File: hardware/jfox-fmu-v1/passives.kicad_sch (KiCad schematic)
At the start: 62 parts, among them X1 16MHz, X2 32.768kHz

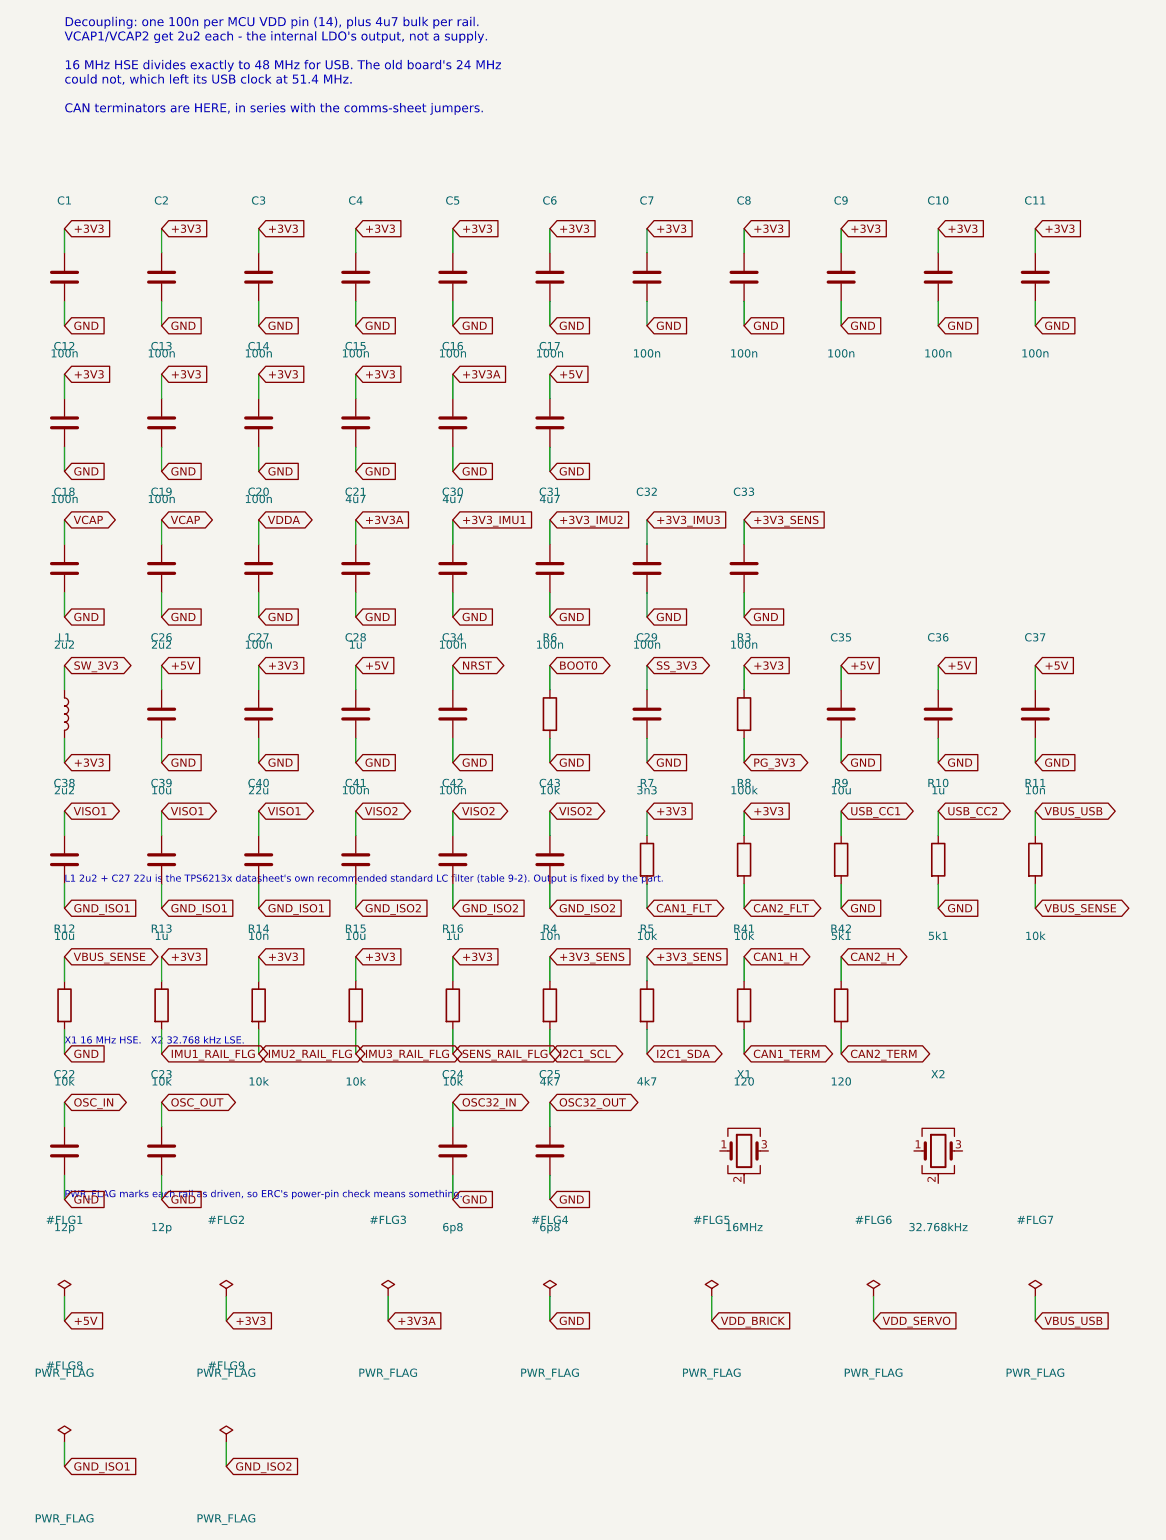
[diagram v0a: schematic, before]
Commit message: Connectors, and three more wires that went nowhere
Eleven headers on a new sheet, Pixhawk pinouts on JST-GH 1.25 mm: two TELEM,
two GPS, RC, a 10-way debug, external SPI, both power inputs, safety switch,
and the eight PWM channels. Pixhawk's pinout rather than a novel one because
the ecosystem's GPS units, radios and power modules are built to it, and a
different pinout means a custom loom for every peripheral.

Isolated nets 48 -> 10.

Three more defects found on the way, all the same shape as the last batch -
something that looked wired and was not:

  C20 decoupled a net called "VDDA" that nothing else joined. The MCU's VDDA
  pin is on +3V3A. The analog rail's bypass capacitor was connected to
  nothing at all.

  LED_R/G/B had MCU pins allocated and drove nothing - the board had no way
  to say anything. Now three LEDs with series resistors, common anode.

  And the two_pin helper assumed every two-pin part is drawn vertically. It
  splits the pins on dy < 0, but Device:LED is horizontal with both pins at
  dy = 0, so both took the same net: D1 shorted its own anode to its cathode
  while the anode net kept only the series resistor. It looked wired and was
  a short. Now split on whichever axis actually separates the pins.

The debug header went from 6 ways to 10. Six could carry SWD and USART1_TX
but not RX, so the console would have been write-only.

Worth recording: when the passives sheet outgrew A4 mid-change, the generator
correctly refused to write - and every checker then passed against the
PREVIOUS generation still on disk. Green on stale files. The fix was to
re-lay-out and regenerate before trusting any of it, but the trap is real and
worth knowing about.

Remaining 10 isolated nets are honest and all blocked on the same two things:
UV1-3_SET and OV1-3_SET need the LTC4417's threshold equations, PGATE1-3 need
its external PMOS pass devices, and both need the datasheet, which would not
download in this session. SD_DETECT needs a socket symbol that ex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
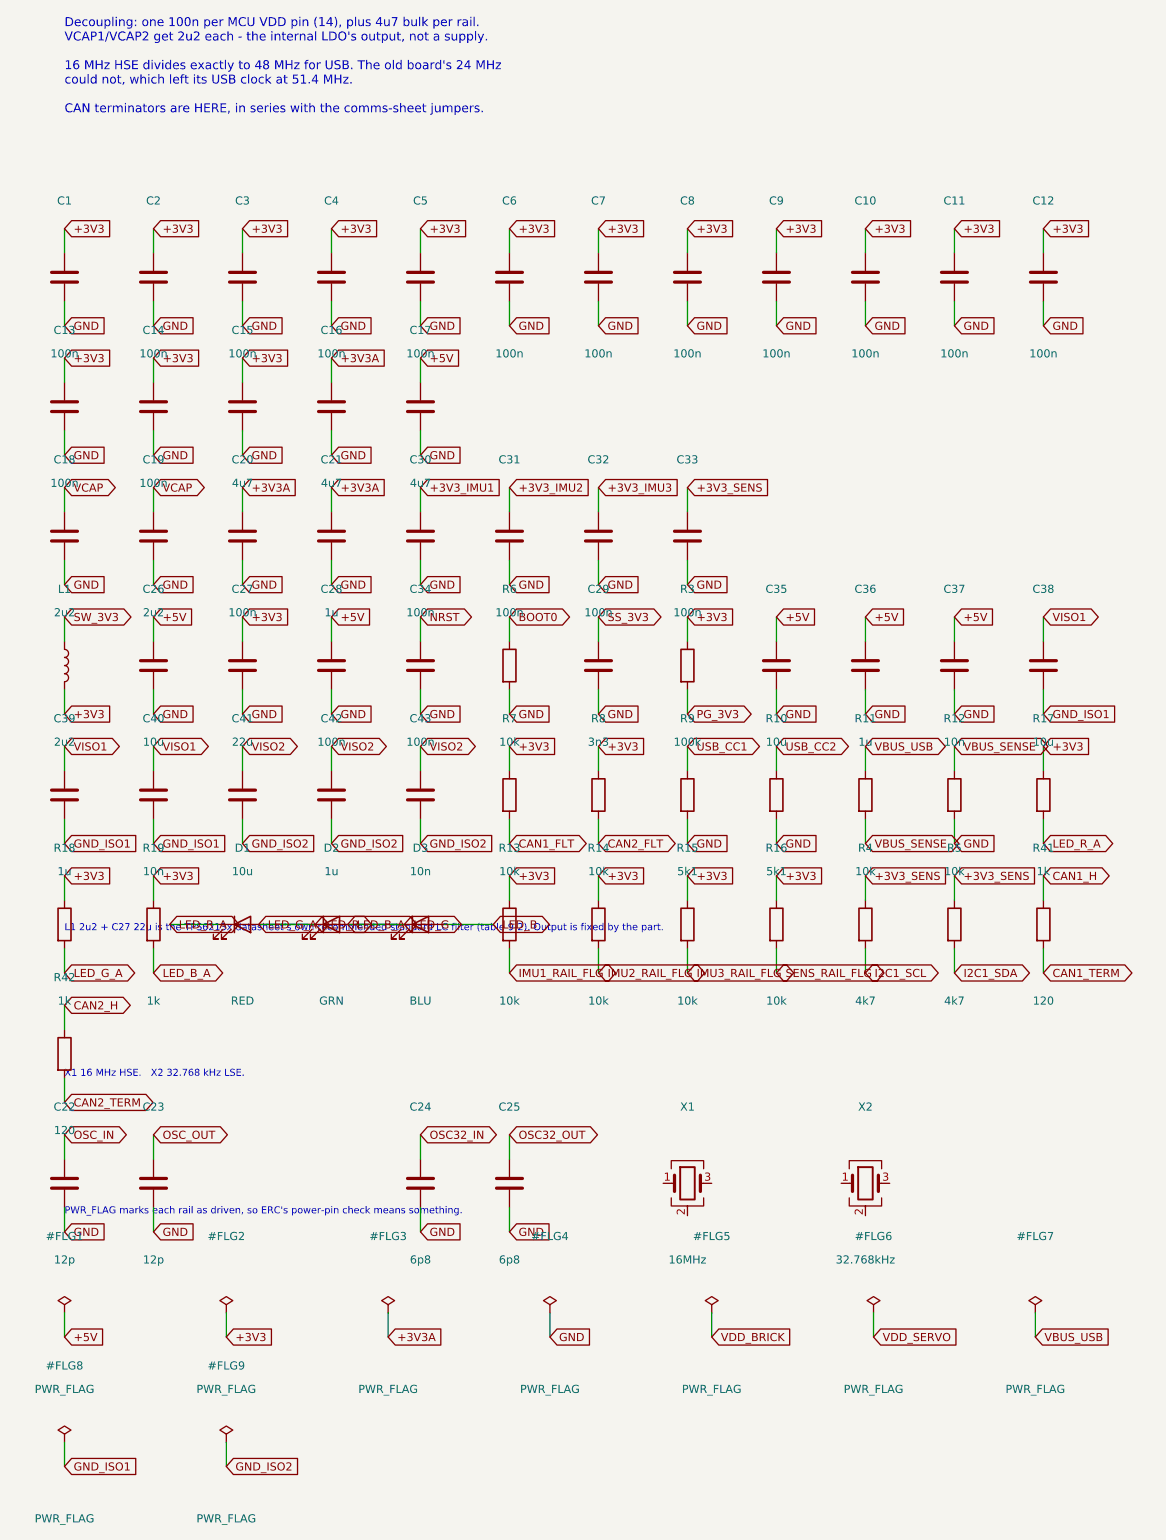
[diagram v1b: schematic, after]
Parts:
- added D1: RED, LED_SMD:LED_0603_1608Metric, symbol Device:LED
- added D2: GRN, LED_SMD:LED_0603_1608Metric, symbol Device:LED
- added D3: BLU, LED_SMD:LED_0603_1608Metric, symbol Device:LED
- added R17, R18, R19: 1k, Resistor_SMD:R_0402_1005Metric, symbol Device:R
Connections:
- net VDDA is gone; now on net +3V3A: C20.1
- net +3V3: now also R17.1, R18.1, R19.1
- new net LED_B: D3.2 (A)
- new net LED_B_A: D2.2 (A), D3.1 (K), R19.2
- new net LED_G_A: D1.2 (A), D2.1 (K), R18.2
- new net LED_R_A: D1.1 (K), R17.2

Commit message: The ORing controller had no switches and no thresholds
With the LTC4417 datasheet in hand, the last of the connections close.
Isolated nets 10 -> 1.

PGATE1-3 drove nothing and UV/OV_SET went nowhere, so U20 sat on the board
arbitrating between three inputs it could neither measure nor switch. Both
halves are now built:

Two back-to-back PMOS per input, sources common, gates both on Gn. That is
what "blocks reverse AND cross conduction" on the datasheet's front page
actually requires - one FET's body diode faces each way. A single FET per
channel leaves a permanent diode path and the ORing does nothing.

And VS1-3 were wired straight to the input rails. VSn senses the FET common
source (ADI figure 1), so the design was measuring the wrong side of a switch
that did not exist.

Thresholds from ADI's equations, with UV taking the middle tap and OV the
bottom one:

    UV = Rtot / (Rmid + Rbot)        OV = Rtot / Rbot

Checked by reproducing the datasheet's own worked example before using them:
806k/39.2k/60.4k gives 9.09 V and 14.99 V, which is what figure 1 labels for a
12 V adapter. Then applied per input - brick 4.52/5.81 V, servo 4.54/6.55 V
because BECs are commonly 5 V or 6 V, USB 4.38/5.47 V.

Two BOM errors the datasheet also settled:

The LTC4417 is a 24-lead part. It carried Package_SO:SSOP-16 - a real
footprint, a real name, eight pads short, and unbuildable. check_fmu_footprints
was verifying that a name RESOLVES, never that it matches the part, so this
passed every run. It now compares pad count against pin count.

That check concealed itself twice while being written, in the way this file
has form for: `mismatched` was not added to the total, so the count silently
dropped by one and printed PASS; then `good` did not include it either, so it
printed FAIL and exited 0. Both fixed, and the total now carries a comment
saying why every failure category must be in it.

And the datasheet's ordering table lists only I (-40/+85) and H (-40/+125)
grades - there is 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
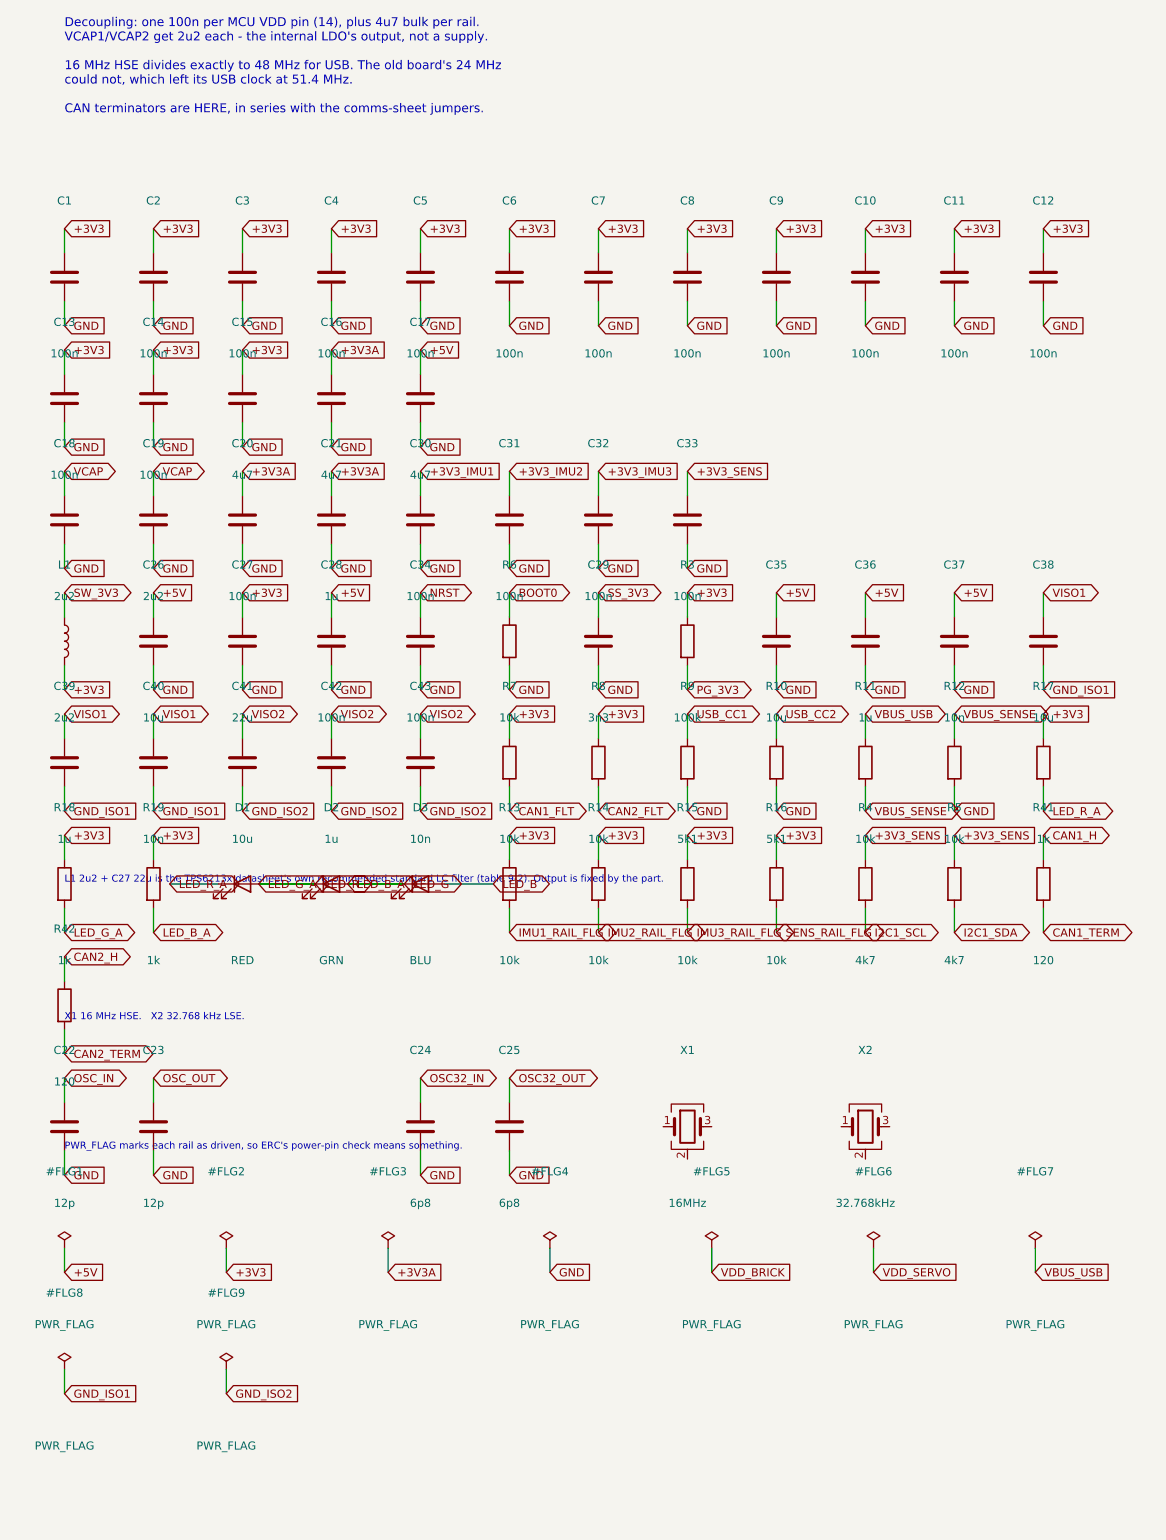
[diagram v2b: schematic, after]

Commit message: microSD with card detect, and the storage split made explicit
The socket was already on the board and every SDMMC line was wired, but it
used Connector:SD_Card_Device - a symbol with no card-detect pin and no
shield. SD_DETECT therefore had an MCU pin allocated and no source, and the
shield floated.

Swapped to Connector:Micro_SD_Card_Det_Hirose_DM3AT, which is the same socket
the footprint was already chosen for and exposes the DET_A/DET_B mechanical
switch plus SHIELD. DET_B grounds, DET_A is pulled up and read, so firmware
can tell "no card" from "card present but failing". Those need different
responses - the first is a pre-flight nag, the second is a logging fault - and
without card detect they are indistinguishable.

Six pull-ups added. The SD specification requires CMD and DAT0-3 held high,
and DAT3 doubles as the card's own detect pin so it must not float during
initialisation. The STM32's internal pull-ups exist but are weak and only
come up after GPIO configuration, which is after the card has already sampled
the bus.

Isolated nets: 1 -> 0. Every net on this board now reaches at least two pins.

On what the card is FOR, since the request was about parameters: it is not
where parameters go, and it should not be.

Parameters and calibration stay in the FM25V02A FRAM, which is where
flight::calibration::storage already writes them - with a "JFOX" magic word
and an FNV-1a checksum so a blank or corrupted record can never read as
valid. FRAM has unlimited write endurance, needs no filesystem, and cannot be
corrupted by power loss mid-write. An SD card can be pulled out, wears out,
and corrupts on power loss during a block write. Putting calibration there
would be a downgrade dressed as convenience.

The card is for flight logs: large, sequential, expendable - the opposite of
parameters, and exactly what the medium is good at. HWR-IFC-006 now says
FRAM explicitly rather than "non-volatile storage", and HWR-IFC-007 covers
the socket, so the distinction is record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
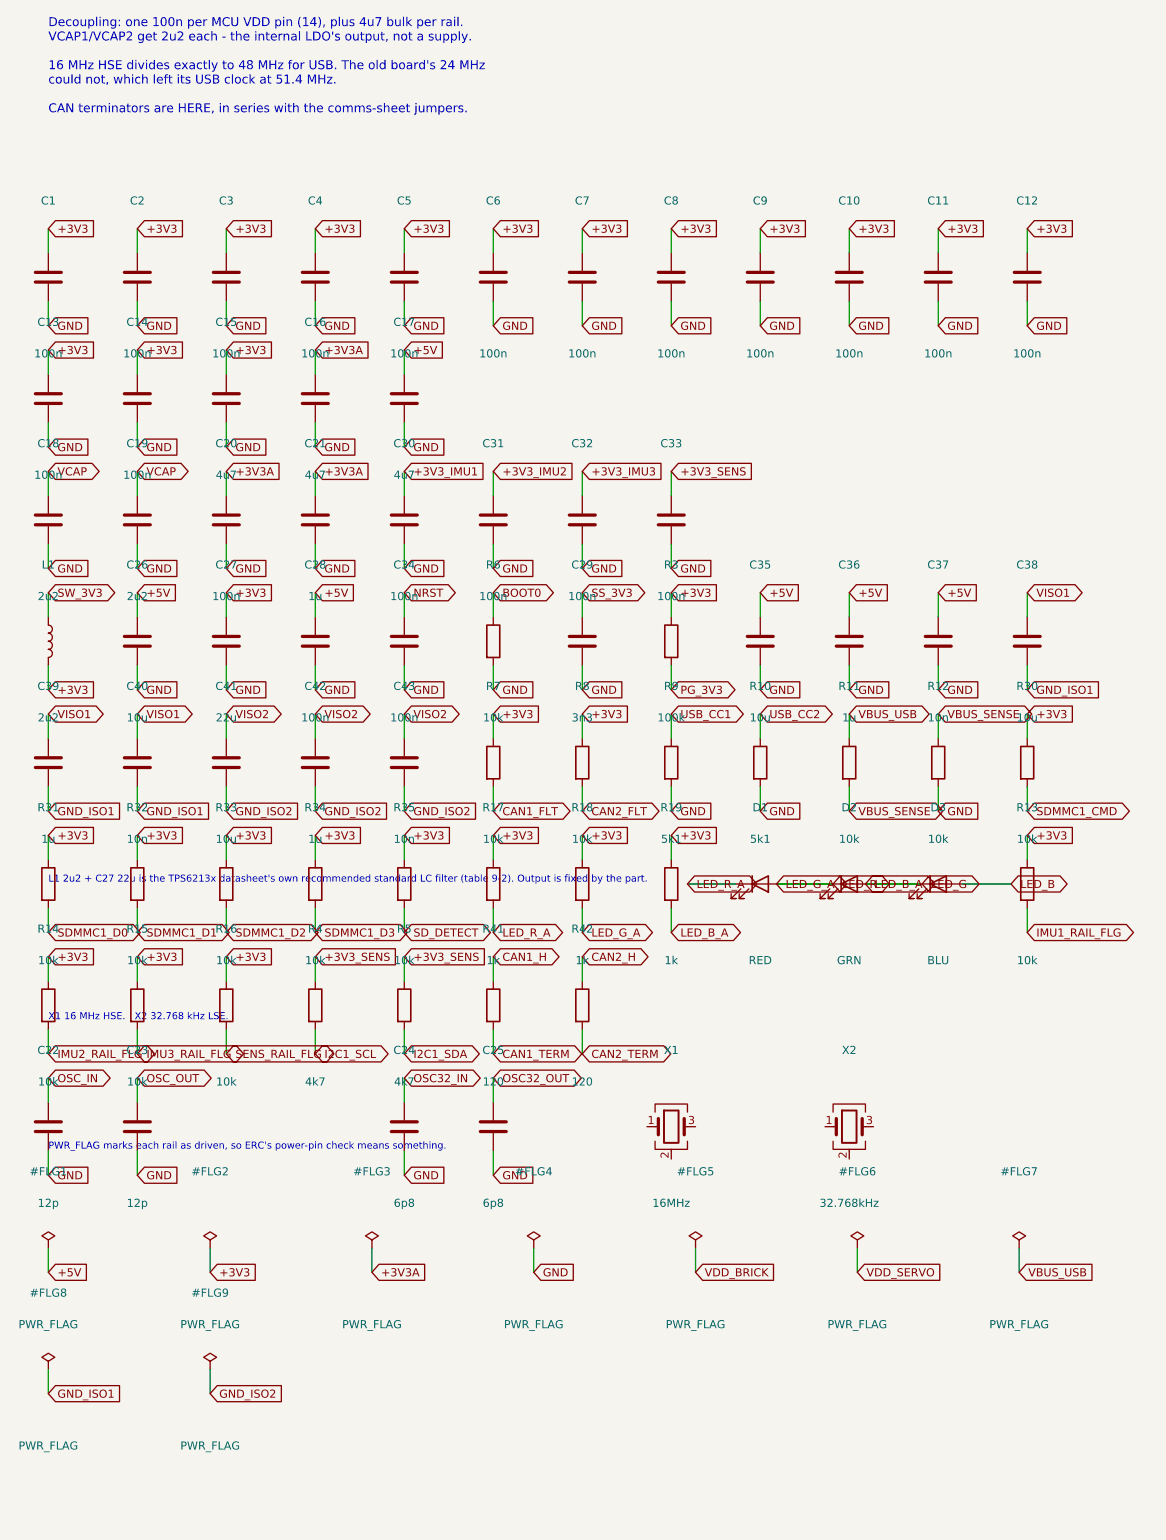
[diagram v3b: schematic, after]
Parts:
- added R30, R31, R32, R33, R34, R35: 10k, Resistor_SMD:R_0402_1005Metric, symbol Device:R
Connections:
- net +3V3: now also R30.1, R31.1, R32.1, R33.1, R34.1, R35.1
- new net SDMMC1_CMD: R30.2
- new net SDMMC1_D0: R31.2
- new net SDMMC1_D1: R32.2
- new net SDMMC1_D2: R33.2
- new net SDMMC1_D3: R34.2
- new net SD_DETECT: R35.2
